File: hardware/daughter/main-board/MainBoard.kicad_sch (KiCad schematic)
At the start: 15 parts, among them J1 Conn_01x03_Pin, J2 Conn_01x03_Pin, J3 Conn_01x03_Pin, J4 Conn_01x03_Pin, SW1 SW_SP3T, SW2 SW_SP3T, U1 CD22M3494MQZ, U2 LM7321MAX/NOPB, U3 TL071, U4 TL071, U5 TL071, U6 TL071

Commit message: Updated daughter board schematic
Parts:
- removed F1, F2, F3: 500mA, Fuse:Fuse_0603_1608Metric_Pad1.05x0.95mm_HandSolder, symbol Device:Fuse
- removed J1, J2, J3, J4: Conn_01x03_Pin, Connector_PinHeader_2.54mm:PinHeader_1x03_P2.54mm_Vertical, symbol Connector:Conn_01x03_Pin
- removed SW1, SW2: SW_SP3T, Button_Switch_THT:SW_Slide_SP3T_Straight_CK_OS103012MU1QP1, symbol SeniorDesign:SW_SP3T_2P
- removed U1: CD22M3494MQZ, SeniorDesignFP:PLCC44_16P66X16P66_INR-M, symbol SeniorDesign:CD22M3494MQZ
- removed U2: LM7321MAX/NOPB, Package_SO:SOIC-8_3.9x4.9mm_P1.27mm, symbol Amplifier_Operational:TL081
- removed U3, U4, U5, U6: TL071, Package_SO:SOIC-8_3.9x4.9mm_P1.27mm, symbol Amplifier_Operational:TL071
- added U11, U12, U47, U51: CD22M3494MQZ, SeniorDesignFP:PLCC44_16P66X16P66_INR-M, symbol SeniorDesign:CD22M3494MQZ
- added U19, U39, U43, U7: ADG1414BRU, Package_SO:TSSOP-24_4.4x7.8mm_P0.65mm, symbol Analog_Switch:ADG1414BRU
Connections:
- net +5V: now also U19.2 (VDD), U39.2 (VDD), U43.2 (VDD), U7.2 (VDD)
- net -5V: now also U19.21 (VSS), U39.21 (VSS), U43.21 (VSS), U7.21 (VSS)
- net GND: now also U19.4 (GND), U39.4 (GND), U43.4 (GND), U7.4 (GND)
- new net A0: U12.32 (Y0), U39.6 (D1), U43.5 (S1)
- new net A1: U12.35 (Y1), U39.8 (D2), U43.7 (S2)
- new net A2: U12.37 (Y2), U39.10 (D3), U43.9 (S3)
- new net A3: U12.39 (Y3), U39.12 (D4), U43.11 (S4)
- new net A4: U12.17 (Y4), U39.13 (D5), U43.14 (S5)
- new net A5: U12.15 (Y5), U39.15 (D6), U43.16 (S6)
- new net A6: U12.13 (Y6), U39.17 (D7), U43.18 (S7)
- new net A7: U12.10 (Y7), U39.19 (D8), U43.20 (S8)
- new net B0: U43.6 (D1), U47.32 (Y0), U7.5 (S1)
- new net B1: U43.8 (D2), U47.35 (Y1), U7.7 (S2)
- new net B2: U43.10 (D3), U47.37 (Y2), U7.9 (S3)
- new net B3: U43.12 (D4), U47.39 (Y3), U7.11 (S4)
- new net B4: U43.13 (D5), U47.17 (Y4), U7.14 (S5)
- new net B5: U43.15 (D6), U47.15 (Y5), U7.16 (S6)
- new net B6: U43.17 (D7), U47.13 (Y6), U7.18 (S7)
- new net B7: U43.19 (D8), U47.10 (Y7), U7.20 (S8)
- new net C0: U19.5 (S1), U7.6 (D1)
- new net C1: U19.7 (S2), U7.8 (D2)
- new net C2: U19.9 (S3), U7.10 (D3)
- new net C3: U19.11 (S4), U7.12 (D4)
- new net C4: U19.14 (S5), U7.13 (D5)
- new net C5: U19.16 (S6), U7.15 (D6)
- new net C6: U19.18 (S7), U7.17 (D7)
- new net C7: U19.20 (S8), U7.19 (D8)
- new net D0: U19.6 (D1), U39.5 (S1), U51.32 (Y0)
- new net D1: U19.8 (D2), U39.7 (S2), U51.35 (Y1)
- new net D2: U19.10 (D3), U39.9 (S3), U51.37 (Y2)
- new net D3: U19.12 (D4), U39.11 (S4), U51.39 (Y3)
- new net D4: U19.13 (D5), U39.14 (S5), U51.17 (Y4)
- new net D5: U19.15 (D6), U39.16 (S6), U51.15 (Y5)
- new net D6: U19.17 (D7), U39.18 (S7), U51.13 (Y6)
- new net D7: U19.19 (D8), U39.20 (S8), U51.10 (Y7)
- new net IO_0: U12.3 (X15)
- new net IO_1: U12.2 (X14)
- new net IO_2: U47.3 (X15)
- new net IO_3: U47.2 (X14)
- new net IO_4: U11.3 (X15)
- new net IO_5: U11.2 (X14)
- new net IO_6: U51.3 (X15)
- new net IO_7: U51.2 (X14)
- no-connect marks 14 -> 0
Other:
- removed sheet MicroController
- removed sheet Power Supply
- removed sheet STD
- removed sheet STD1
- removed sheet STD2
- removed sheet STD3
- note removed: "Controls"
- note removed: "Inputs"
- note removed: "Output Buffers"
- note removed: "Outputs"
- note removed: "Power Supply"
- note removed: "Routing"

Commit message: fixed schematic
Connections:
- net C0: now also U11.32 (Y0)
- net C1: now also U11.35 (Y1)
- net C2: now also U11.37 (Y2)
- net C3: now also U11.39 (Y3)
- net C4: now also U11.17 (Y4)
- net C5: now also U11.15 (Y5)
- net C6: now also U11.13 (Y6)
- net C7: now also U11.10 (Y7)
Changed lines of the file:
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@@
 	(wire
 		(pts
-			(xy 195.58 68.58) (xy 195.58 71.12)
+			(xy 196.85 67.31) (xy 196.85 71.12)
 		)
 		(stroke
@@
 	(wire
 		(pts
-			(xy 180.34 68.58) (xy 180.34 71.12)
+			(xy 181.61 67.31) (xy 181.61 71.12)
 		)
 		(stroke
@@
 	(wire
 		(pts
-			(xy 190.5 68.58) (xy 190.5 71.12)
+			(xy 191.77 67.31) (xy 191.77 71.12)
 		)
 		(stroke
@@
 	(wire
 		(pts
-			(xy 182.88 68.58) (xy 182.88 71.12)
+			(xy 184.15 67.31) (xy 184.15 71.12)
 		)
 		(stroke
@@
 	(wire
 		(pts
-			(xy 185.42 68.58) (xy 185.42 71.12)
+			(xy 186.69 67.31) (xy 186.69 71.12)
 		)
 		(stroke
@@
 	(wire
 		(pts
-			(xy 187.96 68.58) (xy 187.96 71.12)
+			(xy 189.23 67.31) (xy 189.23 71.12)
 		)
 		(stroke
@@
 	(wire
 		(pts
-			(xy 193.04 68.58) (xy 193.04 71.12)
+			(xy 194.31 67.31) (xy 194.31 71.12)
 		)
 		(stroke
@@
 	(wire
 		(pts
-			(xy 177.8 68.58) (xy 177.8 71.12)
+			(xy 179.07 67.31) (xy 179.07 71.12)
 		)
 		(stroke
@@
 	)
 	(label "C7"
-		(at 177.8 68.58 90)
+		(at 179.07 67.31 90)
 		(effects
 			(font
@@
 	)
 	(label "C1"
-		(at 193.04 68.58 90)
+		(at 194.31 67.31 90)
 		(effects
 			(font
@@
 	)
 	(label "C3"
-		(at 187.96 68.58 90)
+		(at 189.23 67.31 90)
 		(effects
 			(font
@@
 	)
 	(label "C5"
-		(at 182.88 68.58 90)
+		(at 184.15 67.31 90)
 		(effects
 			(font
@@
 	)
 	(label "C6"
-		(at 180.34 68.58 90)
+		(at 181.61 67.31 90)
 		(effects
 			(font
@@
 	)
 	(label "C2"
-		(at 190.5 68.58 90)
+		(at 191.77 67.31 90)
 		(effects
 			(font
@@
 	)
 	(label "C0"
-		(at 195.58 68.58 90)
+		(at 196.85 67.31 90)
 		(effects
 			(font
@@
 	)
 	(label "C4"
-		(at 185.42 68.58 90)
-		(effects
-			(font
+		(at 186.69 67.31 90)
+		(effects
+			(font

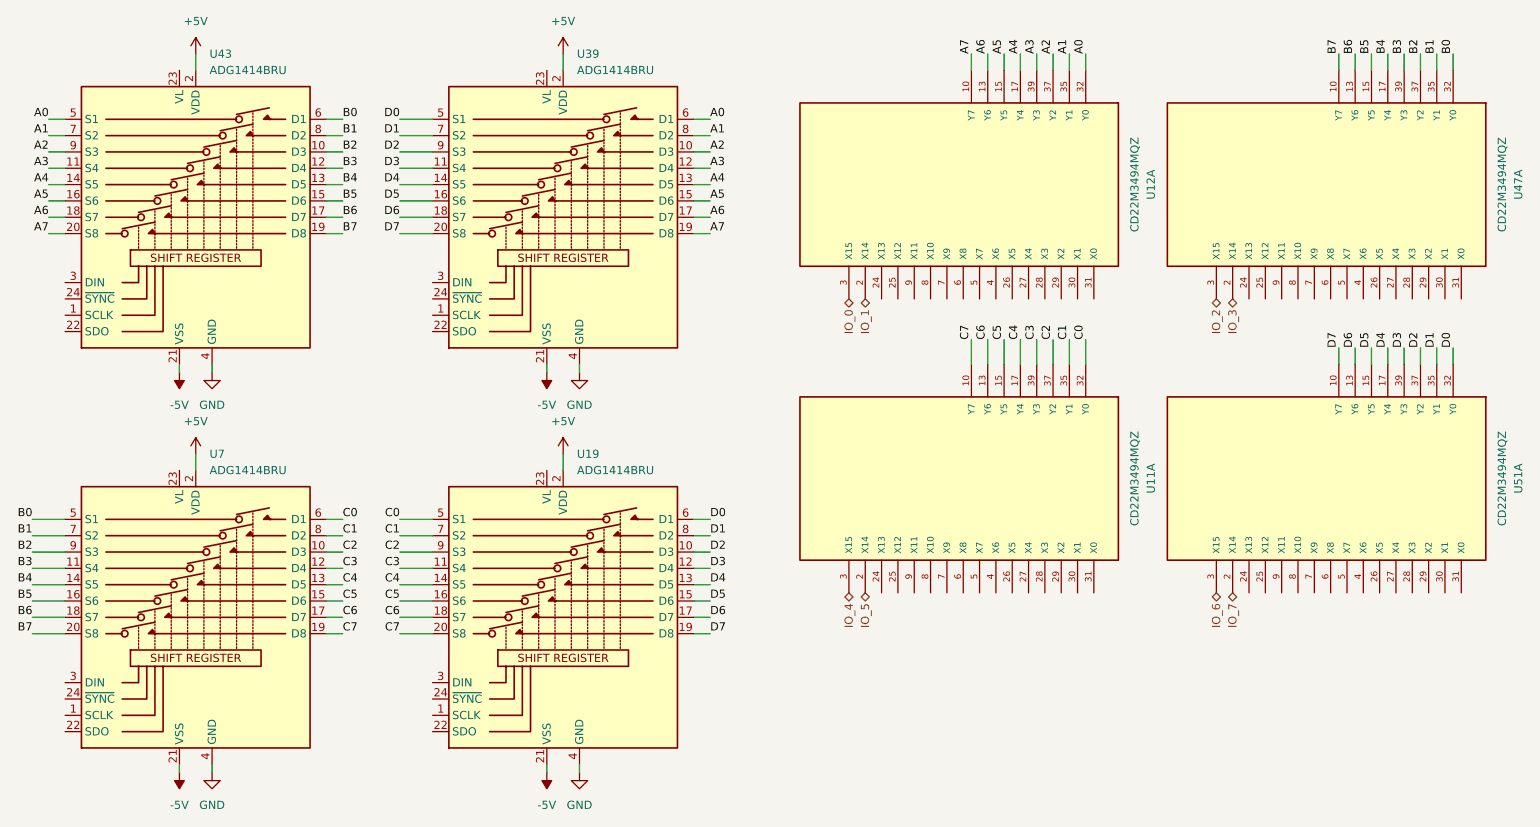
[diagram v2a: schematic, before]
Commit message: formatted heirarchical
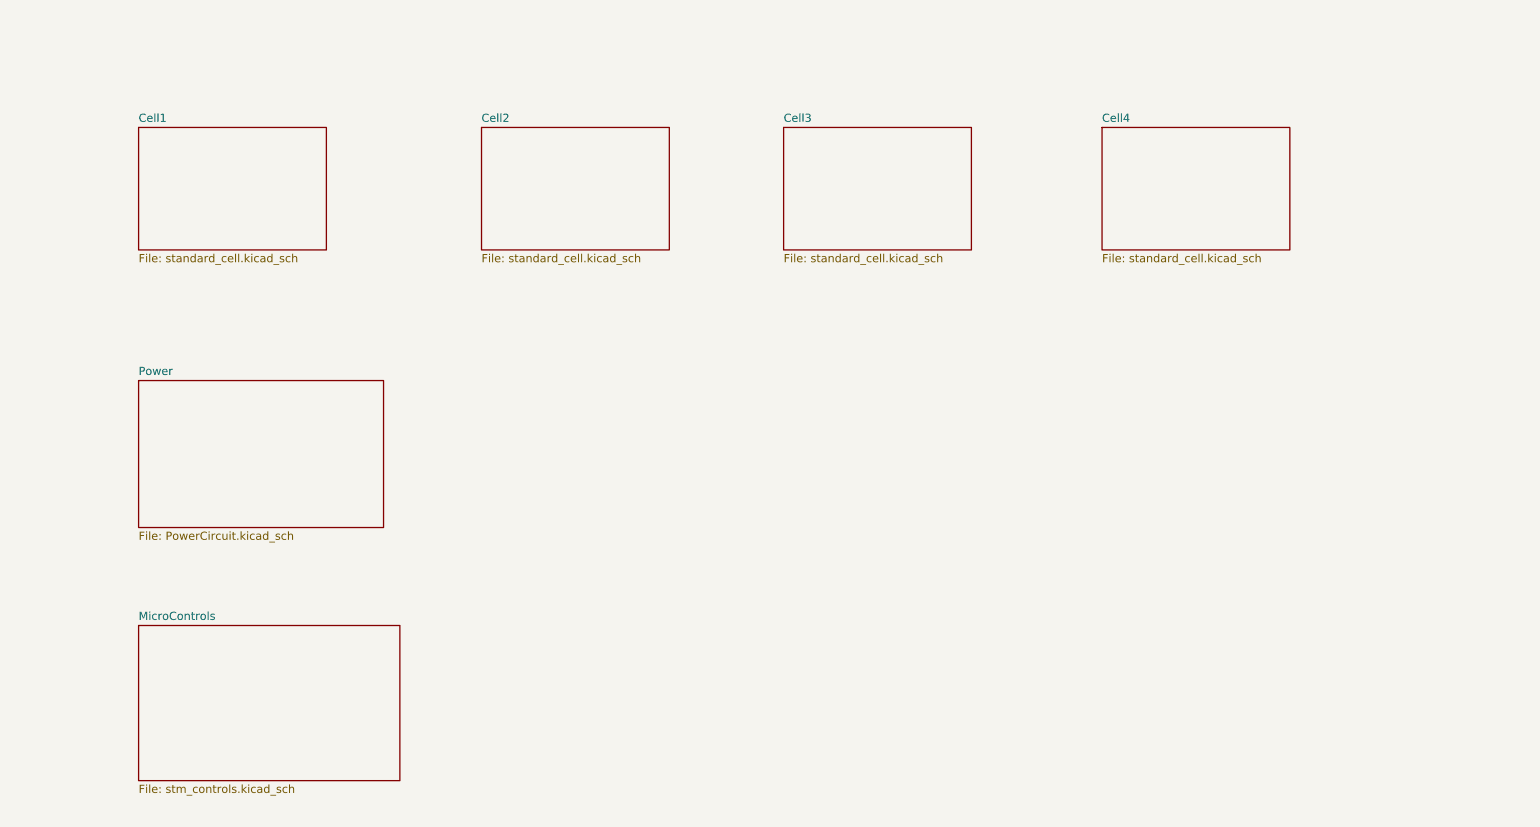
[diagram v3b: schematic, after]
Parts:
- removed U11, U12, U47, U51: CD22M3494MQZ, SeniorDesignFP:PLCC44_16P66X16P66_INR-M, symbol SeniorDesign:CD22M3494MQZ
- removed U19, U39, U43, U7: ADG1414BRU, Package_SO:TSSOP-24_4.4x7.8mm_P0.65mm, symbol Analog_Switch:ADG1414BRU
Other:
- added sheet Cell1 (standard_cell.kicad_sch)
- added sheet Cell2 (standard_cell.kicad_sch)
- added sheet Cell3 (standard_cell.kicad_sch)
- added sheet Cell4 (standard_cell.kicad_sch)
- added sheet MicroControls (stm_controls.kicad_sch)
- added sheet Power (PowerCircuit.kicad_sch)

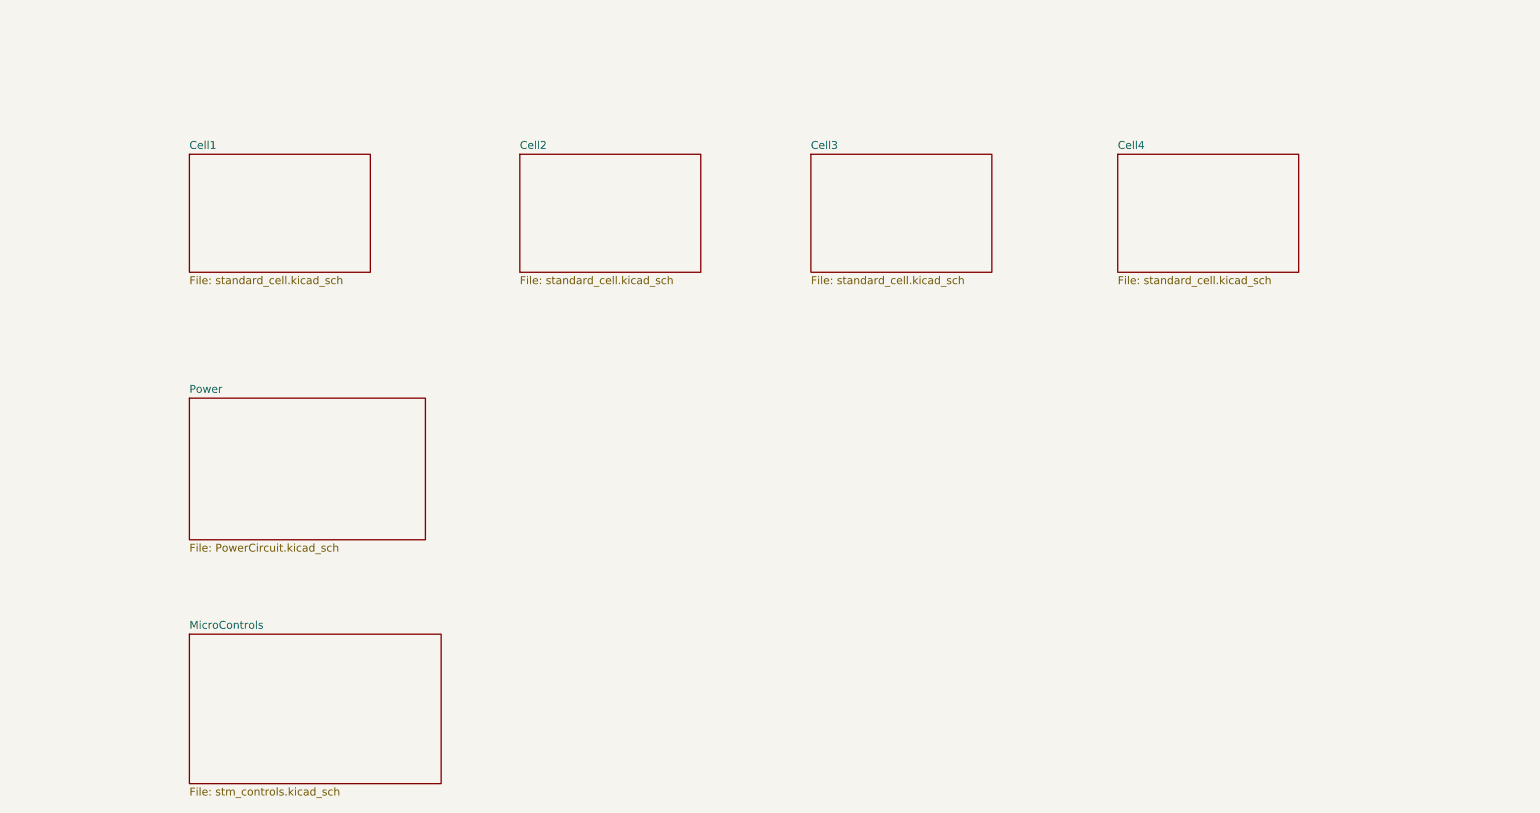
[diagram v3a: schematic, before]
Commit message: Added schematic symbol for analog switches and replaced them in schematic
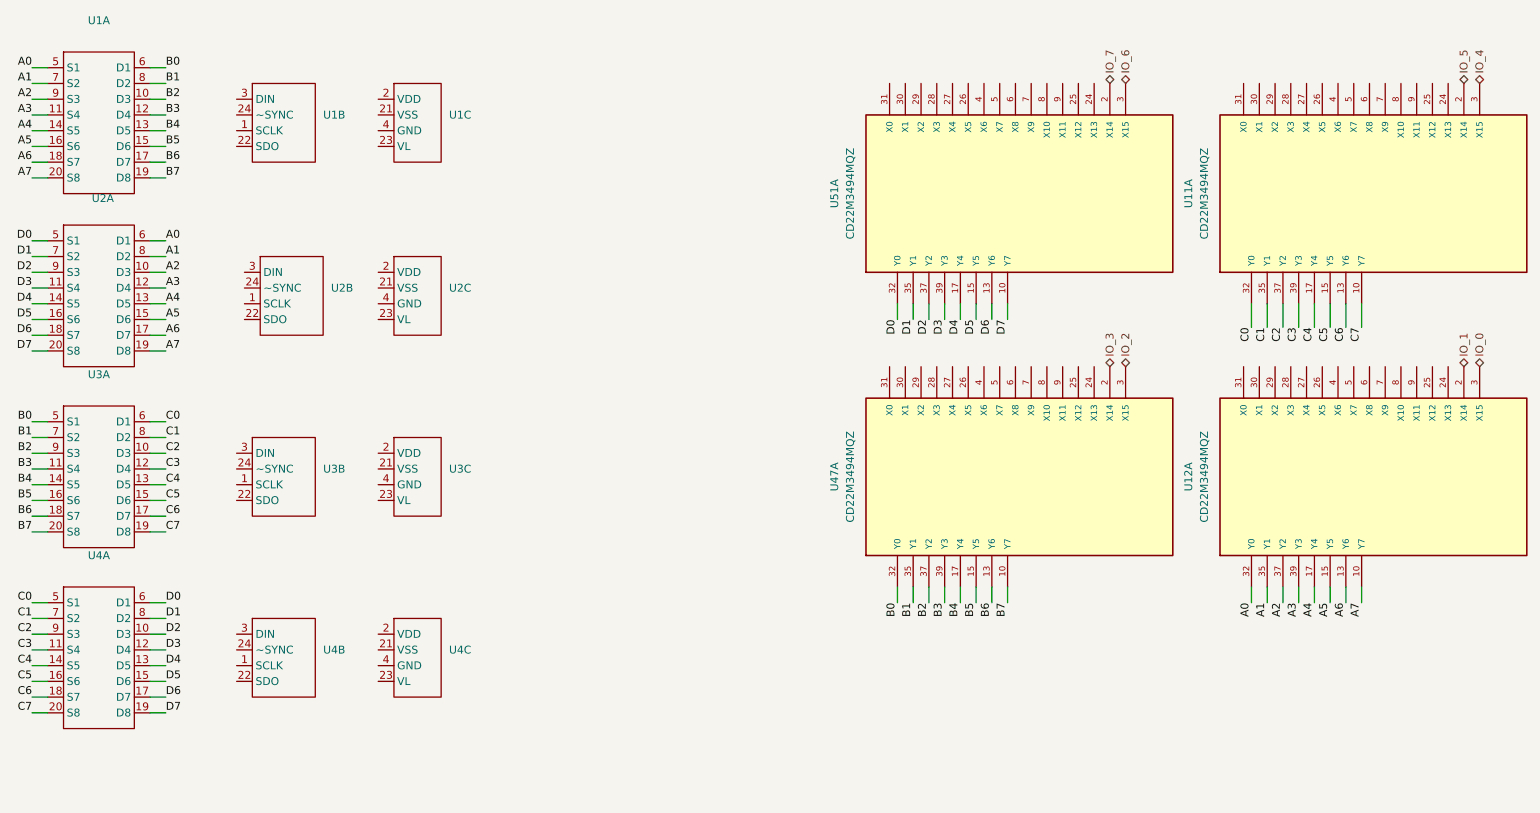
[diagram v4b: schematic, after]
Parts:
- added U1, U2, U3, U4: ~, symbol SeniorDesign:ADG1414BRU_1
- added U11, U12, U47, U51: CD22M3494MQZ, SeniorDesignFP:PLCC44_16P66X16P66_INR-M, symbol SeniorDesign:CD22M3494MQZ
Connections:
- new net A0: U1.5 (S1), U12.32 (Y0), U2.6 (D1)
- new net A1: U1.7 (S2), U12.35 (Y1), U2.8 (D2)
- new net A2: U1.9 (S3), U12.37 (Y2), U2.10 (D3)
- new net A3: U1.11 (S4), U12.39 (Y3), U2.12 (D4)
- new net A4: U1.14 (S5), U12.17 (Y4), U2.13 (D5)
- new net A5: U1.16 (S6), U12.15 (Y5), U2.15 (D6)
- new net A6: U1.18 (S7), U12.13 (Y6), U2.17 (D7)
- new net A7: U1.20 (S8), U12.10 (Y7), U2.19 (D8)
- new net B0: U1.6 (D1), U3.5 (S1), U47.32 (Y0)
- new net B1: U1.8 (D2), U3.7 (S2), U47.35 (Y1)
- new net B2: U1.10 (D3), U3.9 (S3), U47.37 (Y2)
- new net B3: U1.12 (D4), U3.11 (S4), U47.39 (Y3)
- new net B4: U1.13 (D5), U3.14 (S5), U47.17 (Y4)
- new net B5: U1.15 (D6), U3.16 (S6), U47.15 (Y5)
- new net B6: U1.17 (D7), U3.18 (S7), U47.13 (Y6)
- new net B7: U1.19 (D8), U3.20 (S8), U47.10 (Y7)
- new net C0: U11.32 (Y0), U3.6 (D1), U4.5 (S1)
- new net C1: U11.35 (Y1), U3.8 (D2), U4.7 (S2)
- new net C2: U11.37 (Y2), U3.10 (D3), U4.9 (S3)
- new net C3: U11.39 (Y3), U3.12 (D4), U4.11 (S4)
- new net C4: U11.17 (Y4), U3.13 (D5), U4.14 (S5)
- new net C5: U11.15 (Y5), U3.15 (D6), U4.16 (S6)
- new net C6: U11.13 (Y6), U3.17 (D7), U4.18 (S7)
- new net C7: U11.10 (Y7), U3.19 (D8), U4.20 (S8)
- new net D0: U2.5 (S1), U4.6 (D1), U51.32 (Y0)
- new net D1: U2.7 (S2), U4.8 (D2), U51.35 (Y1)
- new net D2: U2.9 (S3), U4.10 (D3), U51.37 (Y2)
- new net D3: U2.11 (S4), U4.12 (D4), U51.39 (Y3)
- new net D4: U2.14 (S5), U4.13 (D5), U51.17 (Y4)
- new net D5: U2.16 (S6), U4.15 (D6), U51.15 (Y5)
- new net D6: U2.18 (S7), U4.17 (D7), U51.13 (Y6)
- new net D7: U2.20 (S8), U4.19 (D8), U51.10 (Y7)
- new net IO_0: U12.3 (X15)
- new net IO_1: U12.2 (X14)
- new net IO_2: U47.3 (X15)
- new net IO_3: U47.2 (X14)
- new net IO_4: U11.3 (X15)
- new net IO_5: U11.2 (X14)
- new net IO_6: U51.3 (X15)
- new net IO_7: U51.2 (X14)
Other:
- removed sheet Cell1
- removed sheet Cell2
- removed sheet Cell3
- removed sheet Cell4
- removed sheet MicroControls
- removed sheet Power

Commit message: Updated SPST symbol
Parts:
- U1, U2, U3, U4: value ~ -> ADG1414BRUZ
- U11, U12, U47, U51: footprint SeniorDesignFP:PLCC44_16P66X16P66_INR-M -> MT8816AF1:QFP80P1200X1200X120-44N
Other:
- moved on the sheet: U11A, U12A, U47A, U51A

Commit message: daughterboard schematic update
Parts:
- added C1: C, symbol Device:C
- added U13: ADG1414BRUZ, symbol SeniorDesign:ADG1414BRU_1
- added U5, U6, U7, U8: TL071, symbol Amplifier_Operational:TL071
- renumbered U47 to U10, U51 to U12, U12 to U9
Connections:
- net OP2C: now reaches U11.24 (X13)
- net OP2C: now also U6.6
- net OP2B: now reaches U11.25 (X12)
- net OP2B: now also U6.2 (-)
- net C7B: now reaches U11.26 (X5)
- net C7A: now reaches U11.27 (X4)
- net R10B: now reaches U11.28 (X3)
- net R10A: now reaches U11.29 (X2)
- net R9B: now reaches U11.30 (X1)
- net R9A: now reaches U11.31 (X0)
- net C8A: now reaches U11.4 (X6)
- net C8B: now reaches U11.5 (X7)
- net OP1A: now reaches U11.6 (X8)
- net OP1A: now also U5.3 (+)
- net OP1B: now reaches U11.7 (X9)
- net OP1B: now also U5.2 (-)
- net OP1C: now reaches U11.8 (X10)
- net OP1C: now also U5.6
- net OP2A: now reaches U11.9 (X11)
- net OP2A: now also U6.3 (+)
- net OP4C: now reaches U12.24 (X13)
- net OP4C: now also U8.6
- net OP4B: now reaches U12.25 (X12)
- net OP4B: now also U8.2 (-)
- net C9B: now reaches U12.26 (X5)
- net C9A: now reaches U12.27 (X4)
- net R12B: now reaches U12.28 (X3)
- net R12A: now reaches U12.29 (X2)
- net R11B: now reaches U12.30 (X1)
- net R11A: now reaches U12.31 (X0)
- net C10A: now reaches U12.4 (X6)
- net C10B: now reaches U12.5 (X7)
- net OP3A: now reaches U12.6 (X8)
- net OP3A: now also U7.3 (+)
- net OP3B: now reaches U12.7 (X9)
- net OP3B: now also U7.2 (-)
- net OP3C: now reaches U12.8 (X10)
- net OP3C: now also U7.6
- net OP4A: now reaches U12.9 (X11)
- net OP4A: now also U8.3 (+)
- net C3B: now reaches U9.24 (X13)
- net C3A: now reaches U9.25 (X12)
- net R3B: now reaches U9.26 (X5)
- net R3A: now reaches U9.27 (X4)
- net R2B: now reaches U9.28 (X3)
- net R2A: now reaches U9.29 (X2)
- net R1B: now reaches U9.30 (X1)
- net R1A: now reaches U9.31 (X0)
- net R4A: now reaches U9.4 (X6)
- net R4B: now reaches U9.5 (X7)
- net C1A: now reaches U9.6 (X8)
- net C1A: now also U13.10 (D3), U13.12 (D4), U13.6 (D1), U13.8 (D2)
- net C1B: now reaches U9.7 (X9)
- net C1B: now also U9.8 (X10), C1.1
- net C2B: now reaches U9.9 (X11)
- net C6B: now reaches U10.24 (X13)
- net C6A: now reaches U10.25 (X12)
- net R7B: now reaches U10.26 (X5)
- net R7A: now reaches U10.27 (X4)
- net R6B: now reaches U10.28 (X3)
- net R6A: now reaches U10.29 (X2)
- net R5B: now reaches U10.30 (X1)
- net R5A: now reaches U10.31 (X0)
- net R8A: now reaches U10.4 (X6)
- net R8B: now reaches U10.5 (X7)
- net C4A: now reaches U10.6 (X8)
- net C4B: now reaches U10.7 (X9)
- net C5B: now reaches U10.8 (X10)
- net C5B: now also U10.9 (X11)
- new net C1S1: C1.2, U13.5 (S1)
- new net C2A: U13.13 (D5), U13.15 (D6), U13.17 (D7), U13.19 (D8)
- new net VDD: U5.7 (V+), U6.7 (V+), U7.7 (V+), U8.7 (V+)
- new net VSS: U5.4 (V-), U6.4 (V-), U7.4 (V-), U8.4 (V-)
- no-connect marks 0 -> 8
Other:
- moved on the sheet: U10A, U1A, U1B, U1C, U2A, U2B, U2C, U3A, U3B, U3C, U4A, U4B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

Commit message: daughterboard updates
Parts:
- added C10, C11, C12, C13, C14, C15, C16, C2, C3, C4, C5, C6, C7, C8, C9: C, symbol Device:C
- added U14: ADG1414BRUZ, symbol SeniorDesign:ADG1414BRU_1
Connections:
- net C1A: now also U14.10 (D3), U14.12 (D4), U14.6 (D1), U14.8 (D2)
- net C1B: now also C10.1, C11.1, C12.1, C2.1, C3.1, C4.1, C9.1
- net C1S1: now also C9.2, U14.5 (S1)
- net C2A: now also U14.13 (D5), U14.15 (D6), U14.17 (D7), U14.19 (D8)
- net C2B: now also C13.1, C14.1, C15.1, C16.1, C5.1, C6.1, C7.1, C8.1
- net C1S4: now reaches U13.11 (S4)
- net C1S4: now also C12.2, C4.2, U14.11 (S4)
- net C2S1: now reaches U13.14 (S5)
- net C2S1: now also C13.2, C5.2, U14.14 (S5)
- net C2S2: now reaches U13.16 (S6)
- net C2S2: now also C14.2, C6.2, U14.16 (S6)
- net C2S3: now reaches U13.18 (S7)
- net C2S3: now also C15.2, C7.2, U14.18 (S7)
- net C2S4: now reaches U13.20 (S8)
- net C2S4: now also C16.2, C8.2, U14.20 (S8)
- net C1S2: now reaches U13.7 (S2)
- net C1S2: now also C10.2, C2.2, U14.7 (S2)
- net C1S3: now reaches U13.9 (S3)
- net C1S3: now also C11.2, C3.2, U14.9 (S3)
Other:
- moved on the sheet: C1, U13A
